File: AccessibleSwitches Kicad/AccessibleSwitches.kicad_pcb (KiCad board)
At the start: 2 copper layers, 30 x 30 mm, 3 parts, among them J1 Conn_01x02_Socket, SW1 D2FS-F-N

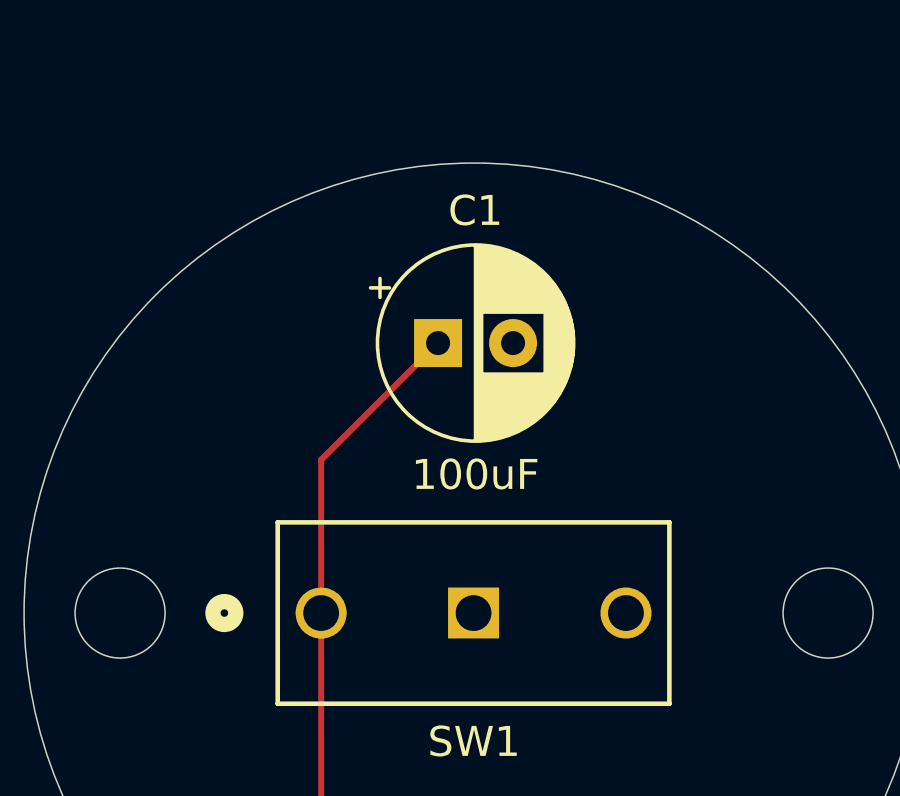
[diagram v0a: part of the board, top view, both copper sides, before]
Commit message: SMD debouncing cap added
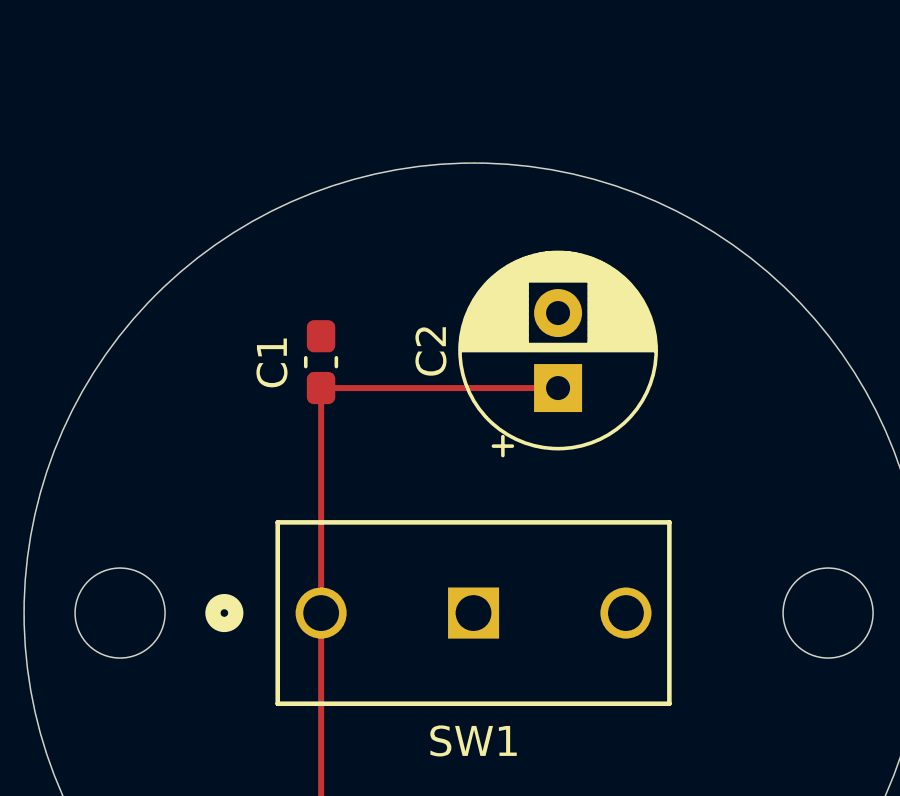
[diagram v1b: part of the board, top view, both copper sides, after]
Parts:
- added C2: 100uF, Capacitor_THT:CP_Radial_D6.3mm_P2.50mm, F.Cu at (151.5, 83.5)
- C1: footprint Capacitor_THT:CP_Radial_D6.3mm_P2.50mm -> Capacitor_SMD:C_0603_1608Metric_Pad1.08x0.95mm_HandSolder
- moved C1 3.95 mm to (143.6, 82.6), turned to 90 degrees
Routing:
- net +3.3V: track 22.2 -> 28.1 mm
